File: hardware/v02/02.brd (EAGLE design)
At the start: 93.7 x 43.8 mm, 30 parts, among them IC1 MSP430G2553, IC2 78L05Z, X2 RJ45-6L-B

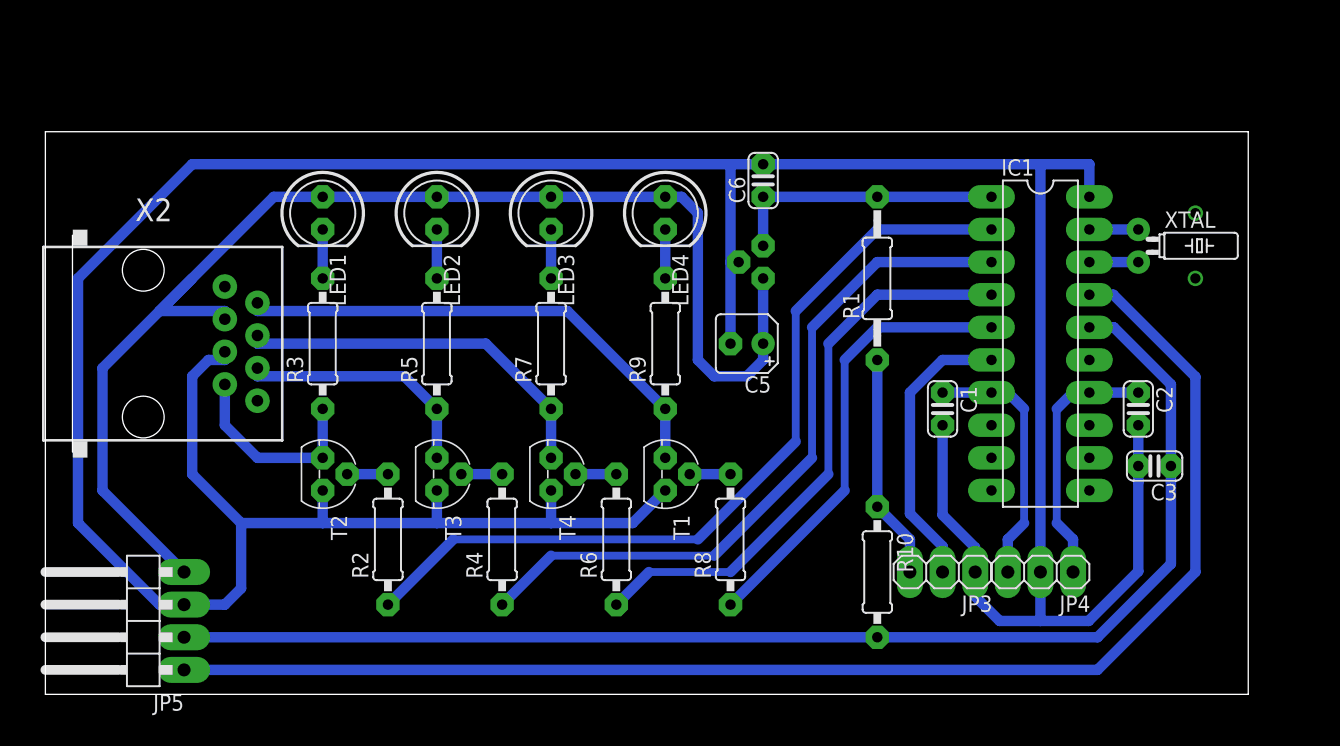
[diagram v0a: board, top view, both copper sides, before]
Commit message: remove/rename some files
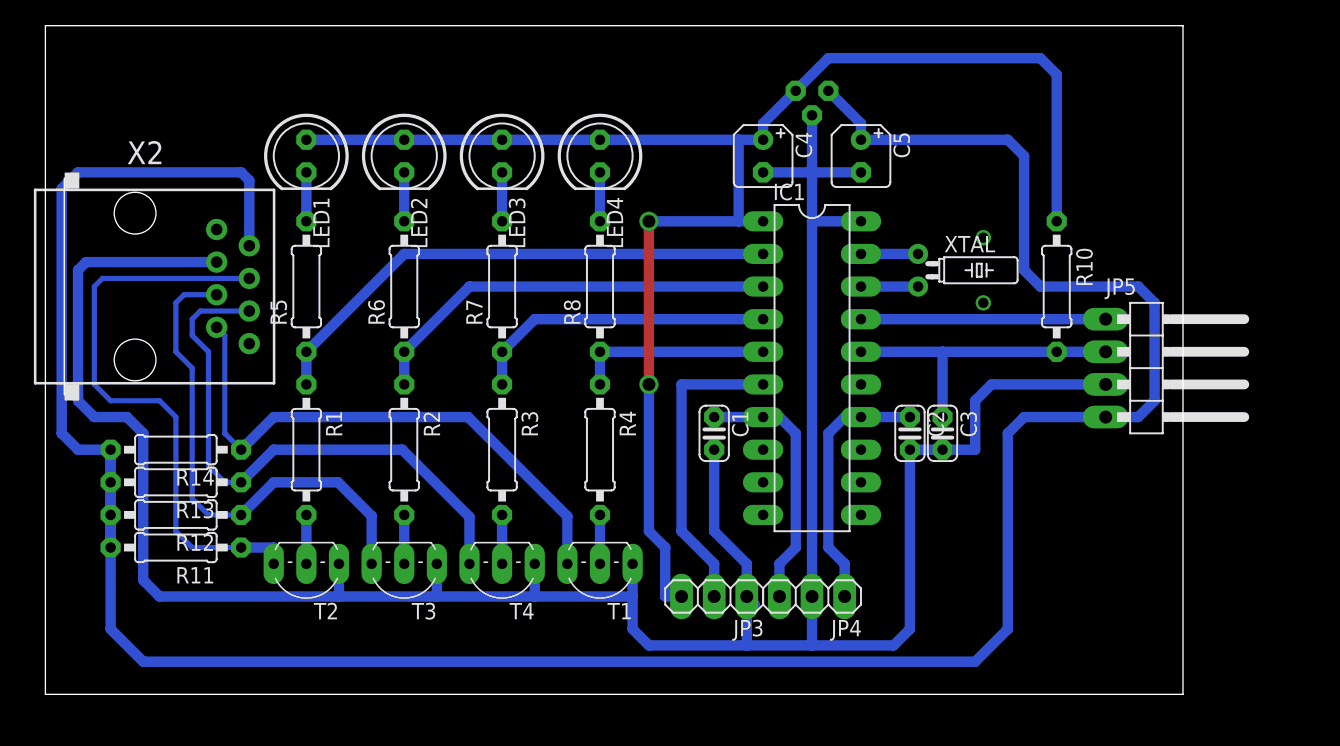
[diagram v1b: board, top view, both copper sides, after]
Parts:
- removed C6: 100nF, rcl:C025-024X044
- removed R9: 220, rcl:0207/10
- added C4: 200nF, rcl:B45181A
- added R11, R12, R13, R14: 10k, rcl:0207/10
- R1: value 0 -> 470; device rcl:0207/12 -> rcl:0207/10
- R3: value 220 -> 470
- R6, R8: value 470 -> 220
- T1, T2, T3, T4: device transistor:TO92 -> transistor:TO92-EBC
- moved JP5 81.8 mm to (86.4, 25.4), turned to 270 degrees
- moved R1 46.4 mm to (20.3, 19.1), turned to 270 degrees
- moved R10 26.3 mm to (78.7, 31.8)
- moved R6 25.7 mm to (27.9, 31.8)
- moved R8 22.2 mm to (43.2, 31.8)
- moved C2 17.9 mm to (67.3, 20.3)
- moved IC1 17.9 mm to (59.7, 25.4)
- moved JP4 17.9 mm to (59.7, 7.62)
- moved C1 17.9 mm to (52.1, 20.3)
- moved JP3 17.9 mm to (52.1, 7.62)
- moved XTAL 17.3 mm to (67.9, 33.0)
- moved C5 17.1 mm to (63.5, 41.9), turned to 270 degrees
- moved C3 16.7 mm to (69.8, 20.3), turned to 270 degrees
- moved R3 16.2 mm to (35.6, 19.1), turned to 270 degrees
- moved IC2 13.9 mm to (59.7, 47.0), turned to 180 degrees
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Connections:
- removed net N$10: R9.1, T1.3, X2.2
- removed net N$14: R3.1, T2.3, X2.7
- removed net N$15: JP3.3, R1.1, R10.1
- removed net N$19: R5.1, T3.3, X2.6
- removed net N$22: R7.1, T4.3, X2.4
- new net N$27: R14.1, T1.C, X2.7
- new net N$28: R13.1, T4.C, X2.6
- new net N$29: R12.1, T3.C, X2.5
- new net N$30: R11.1, T2.C, X2.4
- net +5V: now also R11.2, R12.2, R13.2, R14.2, X2.2; no longer LED1.A, LED2.A, LED3.A, LED4.A, X2.3
- net GND: now also C4.-, T1.E, T2.E, T3.E, T4.E, X2.3; no longer C6.2, T1.1, T2.1, T3.1, T4.1, X2.5
- net N$11: now also R4.2, T1.B; no longer R8.2, T1.2
- net N$12: now also R1.1, R5.1; no longer R2.1
- net N$13: now also R5.2; no longer R3.2
- net N$16: now also R1.2, T2.B; no longer R2.2, T2.2
- net N$17: now also R6.2; no longer R5.2
- net N$20: now also R2.2, T3.B; no longer R4.2, T3.2
- net N$23: now also R3.2, T4.B; no longer R6.2, T4.2
- net N$8: now also R8.2; no longer R9.2
- net N$9: now also R2.1, R6.1; no longer R4.1
- net PB: now also R4.1
- net PR: now also R3.1, R7.1; no longer R6.1
- net VCC: now also C4.+, JP3.3, LED1.A, LED2.A, LED3.A, LED4.A, R10.1; no longer C6.1, R1.2
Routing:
- net +5V: track 104.1 -> 210.9 mm
- net VCC: track 21.6 -> 120.0 mm, vias 0 -> 2
- net N$6: track 108.0 -> 19.0 mm
- net N$5: track 101.4 -> 24.1 mm
- net GND: track 274.4 -> 216.2 mm
- net N$30: track 0.00 -> 45.7 mm
- net N$28: track 0.00 -> 44.4 mm
- net N$27: track 0.00 -> 43.7 mm
- net N$29: track 0.00 -> 39.6 mm
- net N$10: track 39.4 -> 0.00 mm
- net N$22: track 29.4 -> 0.00 mm
- net N$12: track 65.0 -> 41.3 mm
- net N$9: track 55.1 -> 32.6 mm
- net PR: track 45.2 -> 23.9 mm
- net PB: track 35.2 -> 15.2 mm
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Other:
- board size 93.7 x 43.8 mm -> 88.6 x 52.1 mm

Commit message: avoid one wire bridge
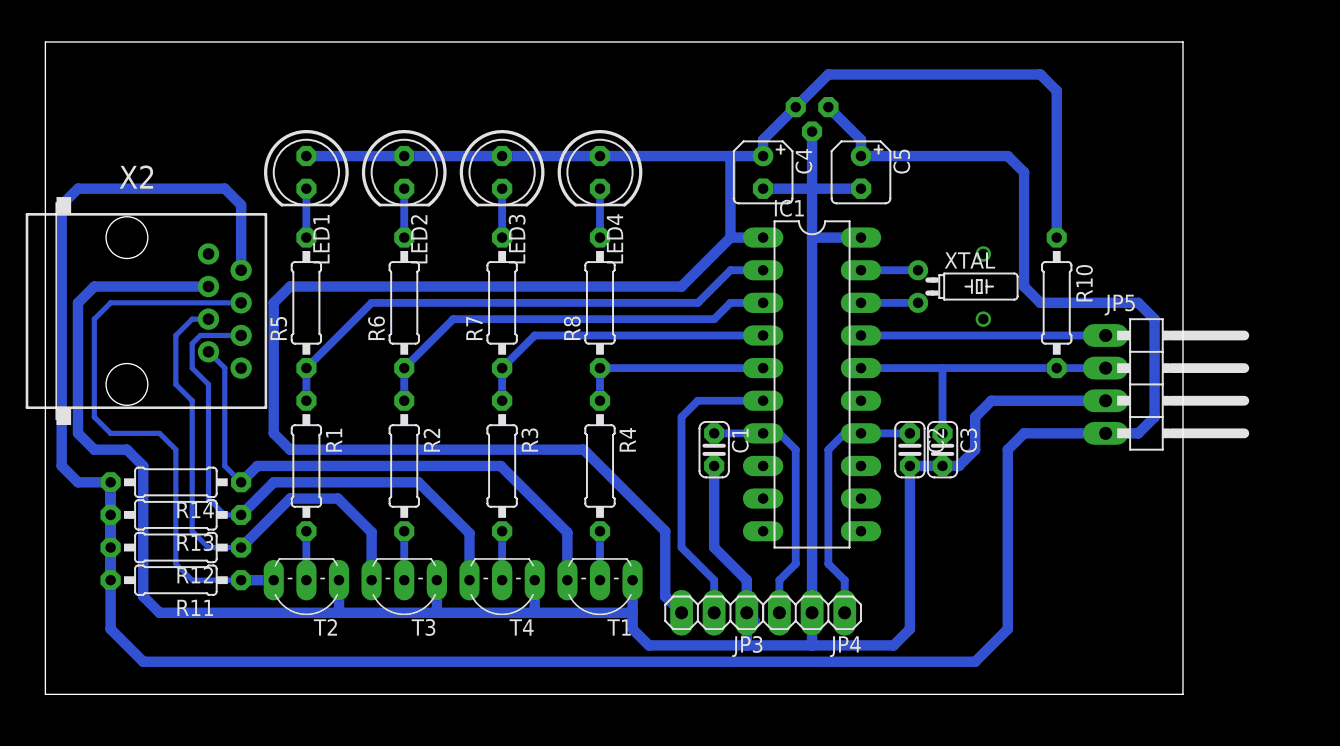
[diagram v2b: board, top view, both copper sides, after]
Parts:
- moved R12 2.54 mm to (10.2, 11.4)
- moved R13 2.54 mm to (10.2, 14.0)
- moved R11 2.54 mm to (10.2, 8.89)
- moved R14 2.54 mm to (10.2, 16.5)
- moved X2 2.01 mm to (6.35, 29.8)
- moved IC2 1.27 mm to (59.7, 45.7)
- moved XTAL 1.27 mm to (67.9, 31.8)
- moved JP3 1.27 mm to (52.1, 6.35)
- moved JP4 1.27 mm to (59.7, 6.35)
- moved T1 1.27 mm to (43.2, 7.62)
- moved T2 1.27 mm to (20.3, 7.62)
- moved T3 1.27 mm to (27.9, 7.62)
- moved T4 1.27 mm to (35.6, 7.62)
- moved C1 1.27 mm to (52.1, 19.1)
- moved C2 1.27 mm to (67.3, 19.1)
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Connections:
- net N$27 renamed OUT4
- net N$28 renamed OUT3
- net N$29 renamed OUT2
- net N$30 renamed OUT1
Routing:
- net VCC: track 120.0 -> 171.0 mm, vias 2 -> 0
- net GND: track 216.2 -> 208.7 mm
- net +5V: track 210.9 -> 208.0 mm
- net OUT1: track 45.7 -> 44.0 mm
- net N$1: track 23.9 -> 23.2 mm
- net OUT4: track 43.7 -> 43.0 mm
- net OUT3: track 44.4 -> 43.9 mm
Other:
- board size 88.6 x 52.1 mm -> 88.6 x 50.8 mm

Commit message: rearrange
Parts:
- removed R11, R12, R13, R14: 10k, rcl:0207/10
- removed R5, R6, R7, R8: 220, rcl:0207/10
- added RN1: 4.7k, resistor-net:RN-5
- added RN2: 220, resistor-net:RN-5
- R1, R10, R2, R3, R4: device rcl:0207/10 -> rcl:0207/12
- moved C5 57.5 mm to (6.35, 34.3), turned to 90 degrees
- moved IC2 48.7 mm to (12.7, 33.0), turned to 0 degrees
- moved C4 37.4 mm to (19.1, 34.3), turned to 90 degrees
- moved R1 30.5 mm to (49.5, 26.7)
- moved LED1 29.5 mm to (49.5, 36.8)
- moved T2 29.0 mm to (48.3, 15.2)
- moved X2 22.9 mm to (12.1, 7.62), turned to 0 degrees
- moved T1 19.3 mm to (25.4, 15.2)
- moved R4 18.8 mm to (26.7, 26.7)
- moved LED4 16.9 mm to (26.7, 36.8)
- moved R2 16.6 mm to (41.9, 26.7)
- moved T3 14.8 mm to (40.6, 15.2)
- moved LED2 14.5 mm to (41.9, 36.8)
- moved R3 8.98 mm to (34.3, 26.7)
- moved T4 8.03 mm to (33.0, 15.2)
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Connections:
- removed net N$17: LED2.K, R6.2
- removed net N$21: LED3.K, R7.2
- new net N$10: LED2.A, RN2.3
- new net N$14: LED4.A, RN2.5
- net +5V: now also RN1.1, X2.3; no longer JP5.4, R11.2, R12.2, R13.2, R14.2, X2.2
- net GND: now also X2.5; no longer X2.3
- net N$12: now also LED1.K; no longer R5.1
- net N$13: now also LED3.A, RN2.4; no longer LED1.K, R5.2
- net N$8: now also LED1.A, RN2.2; no longer LED4.K, R8.2
- net N$9: now also LED2.K; no longer R6.1
- net OUT1: now also RN1.2, X2.2; no longer R11.1, X2.4
- net OUT2: now also RN1.3, X2.4; no longer R12.1, X2.5
- net OUT3: now also RN1.4; no longer R13.1
- net OUT4: now also RN1.5; no longer R14.1
- net PB: now also LED4.K; no longer R8.1
- net PR: now also LED3.K; no longer R7.1
- net VCC: now also JP5.4, RN2.1; no longer LED1.A, LED2.A, LED3.A, LED4.A
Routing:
- net +5V: track 208.0 -> 33.3 mm
- net GND: track 208.7 -> 276.6 mm, vias 0 -> 2
- net VCC: track 171.0 -> 211.4 mm
- net N$12: track 41.3 -> 14.0 mm
- net PB: track 15.2 -> 40.0 mm
- net OUT4: track 43.0 -> 23.2 mm
- net OUT1: track 44.0 -> 58.8 mm
- net OUT3: track 43.9 -> 31.3 mm
- net N$9: track 32.6 -> 22.6 mm
- net N$14: track 0.00 -> 9.94 mm
- net PR: track 23.9 -> 31.3 mm
- net N$8: track 3.81 -> 9.94 mm
- net OUT2: track 39.7 -> 45.1 mm
- net N$5: track 24.1 -> 19.0 mm
- net N$10: track 0.00 -> 4.86 mm
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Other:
- board size 88.6 x 50.8 mm -> 94.9 x 50.8 mm

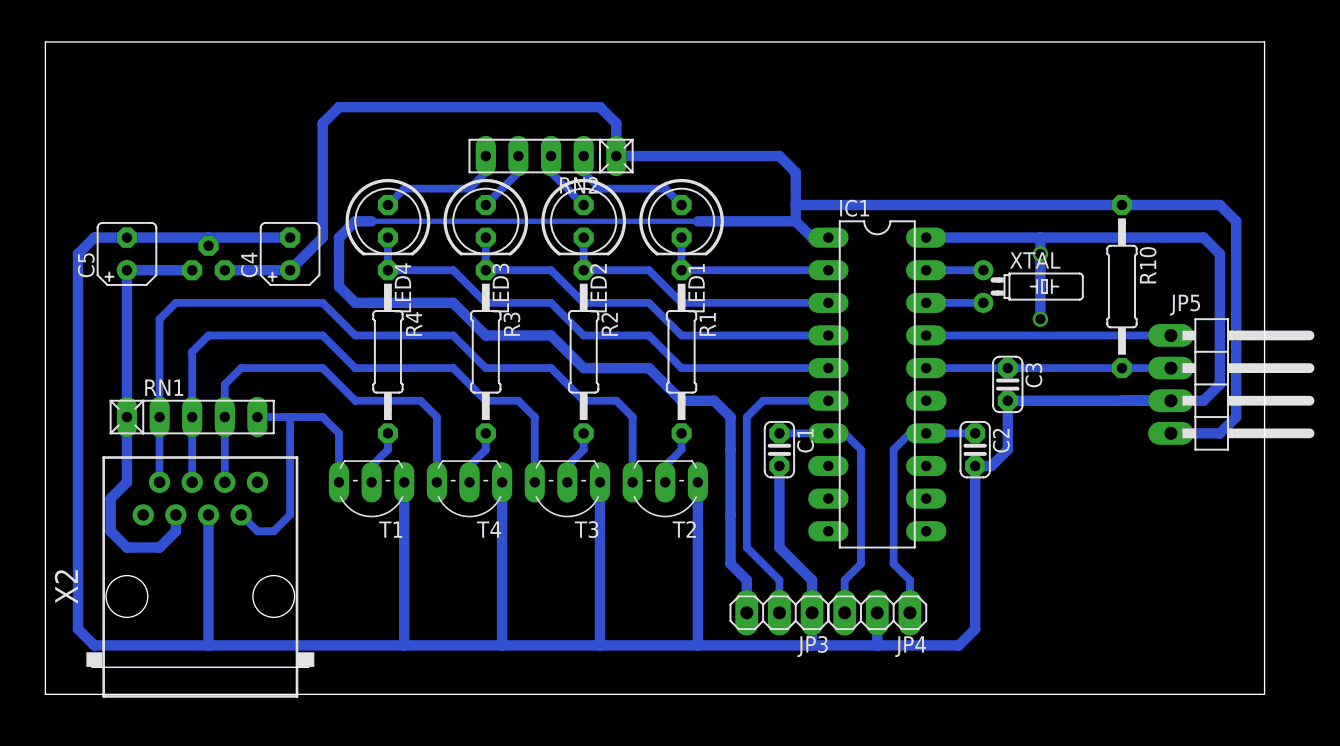
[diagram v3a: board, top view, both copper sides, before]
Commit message: smaller IC; rearrange
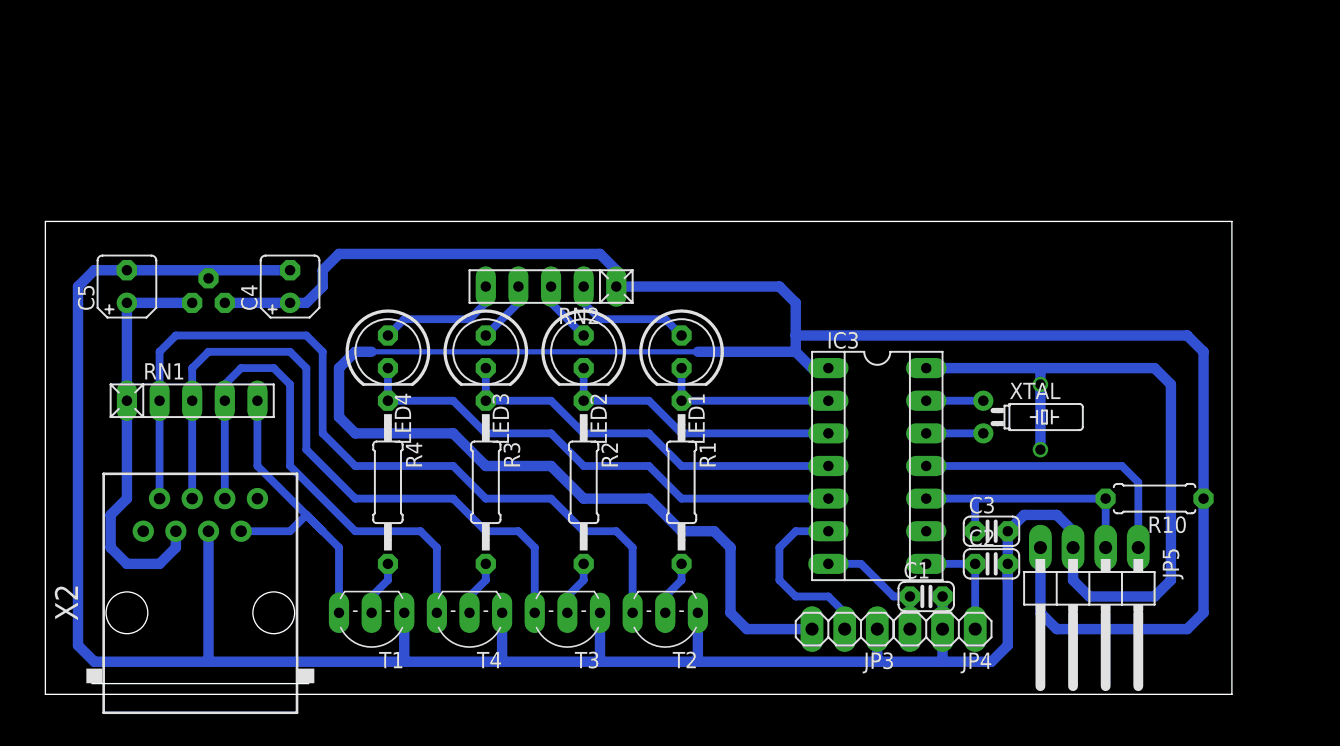
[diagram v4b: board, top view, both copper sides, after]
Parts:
- removed IC1: MSP430G2553, ic-package:DIL20
- added IC3: MSP430G2553, ic-package:SOCKET-14
- R10: device rcl:0207/12 -> rcl:0207/7
- moved JP5 19.4 mm to (81.3, 7.62), turned to 180 degrees
- moved R10 16.7 mm to (86.4, 15.2), turned to 180 degrees
- moved C1 16.2 mm to (68.6, 7.62), turned to 0 degrees
- moved C3 11.5 mm to (73.7, 12.7), turned to 0 degrees
- moved R1 10.2 mm to (49.5, 16.5)
- moved R2 10.2 mm to (41.9, 16.5)
- moved R3 10.2 mm to (34.3, 16.5)
- moved R4 10.2 mm to (26.7, 16.5)
- moved T1 10.2 mm to (25.4, 5.08)
- moved T2 10.2 mm to (48.3, 5.08)
- moved T3 10.2 mm to (40.6, 5.08)
- moved T4 10.2 mm to (33.0, 5.08)
- moved XTAL 10.2 mm to (73.0, 21.6)
- moved LED1 10.2 mm to (49.5, 26.7)
- moved LED2 10.2 mm to (41.9, 26.7)
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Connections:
- net GND: now also IC3.14; no longer IC1.20
- net N$1: now also IC3.6; no longer IC1.6
- net N$12: now also IC3.2; no longer IC1.2
- net N$2: now also IC3.13; no longer IC1.19
- net N$3: now also IC3.7; no longer IC1.7
- net N$4: now also IC3.8; no longer IC1.14
- net N$5: now also IC3.10; no longer IC1.16
- net N$6: now also IC3.11; no longer IC1.17
- net N$7: now also IC3.12; no longer IC1.18
- net N$9: now also IC3.3; no longer IC1.3
- net PB: now also IC3.5; no longer IC1.5
- net PR: now also IC3.4; no longer IC1.4
- net VCC: now also IC3.1; no longer IC1.1
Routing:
- net GND: track 276.6 -> 222.0 mm
- net N$4: track 20.1 -> 8.89 mm
- net N$3: track 20.1 -> 9.94 mm
- net OUT3: track 31.3 -> 40.5 mm
- net N$1: track 23.2 -> 14.3 mm
- net OUT2: track 45.1 -> 52.5 mm
- net OUT1: track 58.8 -> 64.4 mm
- net OUT4: track 23.2 -> 26.5 mm
- net N$6: track 19.0 -> 22.1 mm
- net VCC: track 211.4 -> 213.9 mm
- net +5V: track 33.3 -> 32.1 mm
- net N$5: track 19.0 -> 20.3 mm
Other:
- board size 94.9 x 50.8 mm -> 92.4 x 36.8 mm

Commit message: minor change
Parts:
- moved C2 2.54 mm to (73.7, 7.62)
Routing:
- net OUT4: track 26.5 -> 24.7 mm
- net N$4: track 8.89 -> 8.15 mm
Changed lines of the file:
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@@
 <elements>
 <element name="C1" library="rcl" package="C025-024X044" value="100nF" x="68.58" y="7.62"/>
-<element name="C2" library="rcl" package="C025-024X044" value="100nF" x="73.66" y="10.16"/>
+<element name="C2" library="rcl" package="C025-024X044" value="100nF" x="73.66" y="7.62"/>
 <element name="XTAL" library="crystal" package="TC26H" value="" x="73.025" y="21.59" rot="R270">
 <attribute name="MF" value="" x="73.025" y="21.59" size="1.778" layer="27" rot="R270" display="off"/>
@@
 <wire x1="69.85" y1="2.54" x2="64.77" y2="2.54" width="0.8128" layer="16"/>
 <wire x1="64.77" y1="2.54" x2="64.77" y2="5.08" width="0.8128" layer="16"/>
-<wire x1="74.93" y1="8.89" x2="74.93" y2="10.16" width="0.8128" layer="16"/>
-<wire x1="74.93" y1="10.16" x2="74.93" y2="3.81" width="0.8128" layer="16"/>
+<wire x1="74.93" y1="8.89" x2="74.93" y2="7.62" width="0.8128" layer="16"/>
+<wire x1="74.93" y1="7.62" x2="74.93" y2="3.81" width="0.8128" layer="16"/>
 <wire x1="50.8" y1="6.35" x2="50.8" y2="2.54" width="0.8128" layer="16"/>
 <wire x1="50.8" y1="2.54" x2="64.77" y2="2.54" width="0.8128" layer="16"/>
@@
 <wire x1="78.74" y1="13.97" x2="76.2" y2="13.97" width="0.8128" layer="16"/>
 <wire x1="76.2" y1="13.97" x2="74.93" y2="12.7" width="0.8128" layer="16"/>
-<wire x1="74.93" y1="12.7" x2="74.93" y2="10.16" width="0.8128" layer="16"/>
+<wire x1="74.93" y1="12.7" x2="74.93" y2="7.62" width="0.8128" layer="16"/>
 <wire x1="69.85" y1="7.62" x2="69.85" y2="5.08" width="0.8128" layer="16"/>
 </signal>
@@
 <contactref element="C2" pad="1"/>
 <contactref element="JP4" pad="1"/>
-<wire x1="72.39" y1="5.08" x2="72.39" y2="10.16" width="0.6096" layer="16"/>
+<wire x1="72.39" y1="5.08" x2="72.39" y2="7.62" width="0.6096" layer="16"/>
 <contactref element="IC3" pad="8"/>
-<wire x1="72.39" y1="10.16" x2="68.58" y2="10.16" width="0.6096" layer="16"/>
+<wire x1="72.39" y1="7.62" x2="72.39" y2="8.89" width="0.6096" layer="16"/>
+<wire x1="72.39" y1="8.89" x2="71.12" y2="10.16" width="0.6096" layer="16"/>
+<wire x1="71.12" y1="10.16" x2="68.58" y2="10.16" width="0.6096" layer="16"/>
 </signal>
 <signal name="N$5">
@@
 <wire x1="20.32" y1="13.97" x2="21.59" y2="12.7" width="0.6096" layer="16"/>
 <wire x1="22.86" y1="11.43" x2="21.59" y2="12.7" width="0.6096" layer="16"/>
-<wire x1="21.59" y1="12.7" x2="16.51" y2="17.78" width="0.6096" layer="16"/>
+<wire x1="20.32" y1="13.97" x2="16.51" y2="17.78" width="0.6096" layer="16"/>
 <wire x1="16.51" y1="17.78" x2="16.51" y2="22.86" width="0.6096" layer="16"/>
 </signal>
